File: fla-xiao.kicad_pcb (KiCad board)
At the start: 2 copper layers, 49.7 x 30.7 mm, 9 parts, among them J3 Conn_PinHeader_2x03_P2.54mm_V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, J4 Conn_PinHeader_1x08_P2.54mm_H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, J5 Conn_PinHeader_1x05_P2.54mm_H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, M1 Module_XIAO-RP2040_SocketSMD, SW1 BUTTON_B3SN

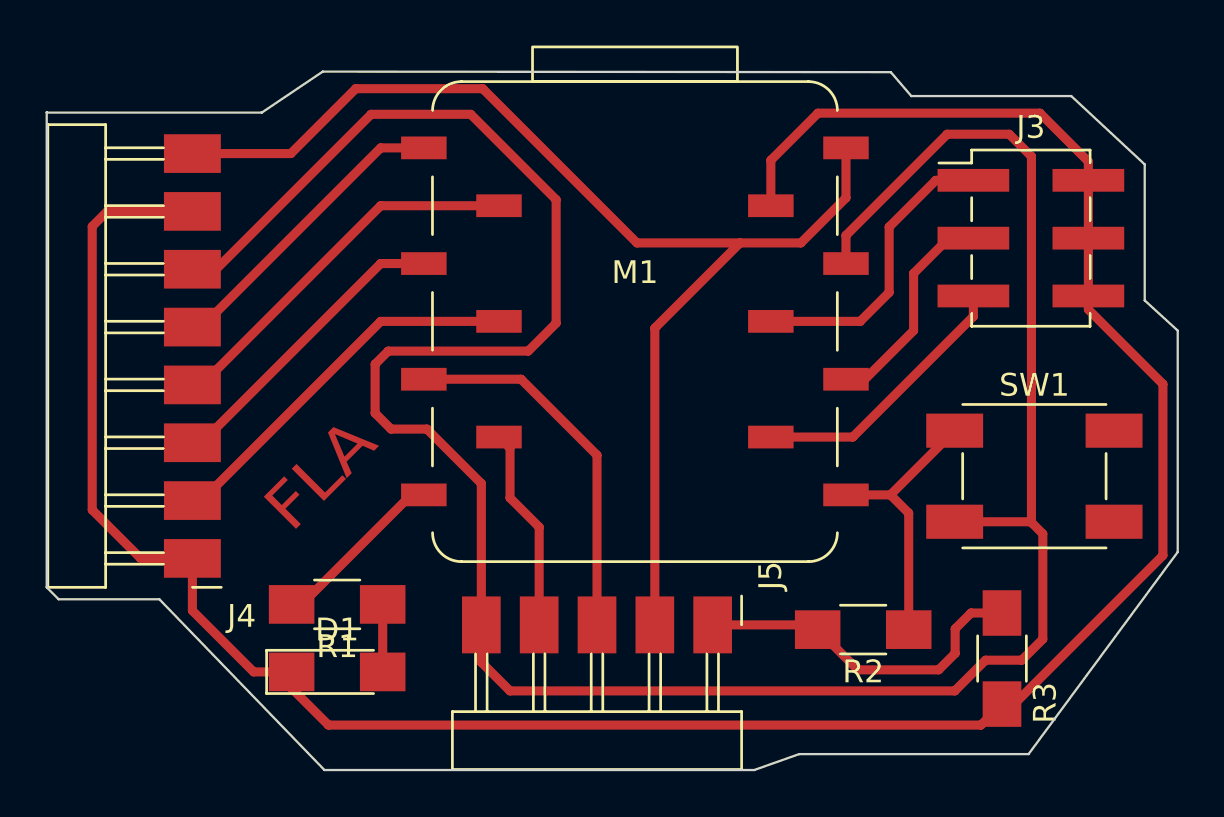
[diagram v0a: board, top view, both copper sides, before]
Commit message: Adjust trace and updated image
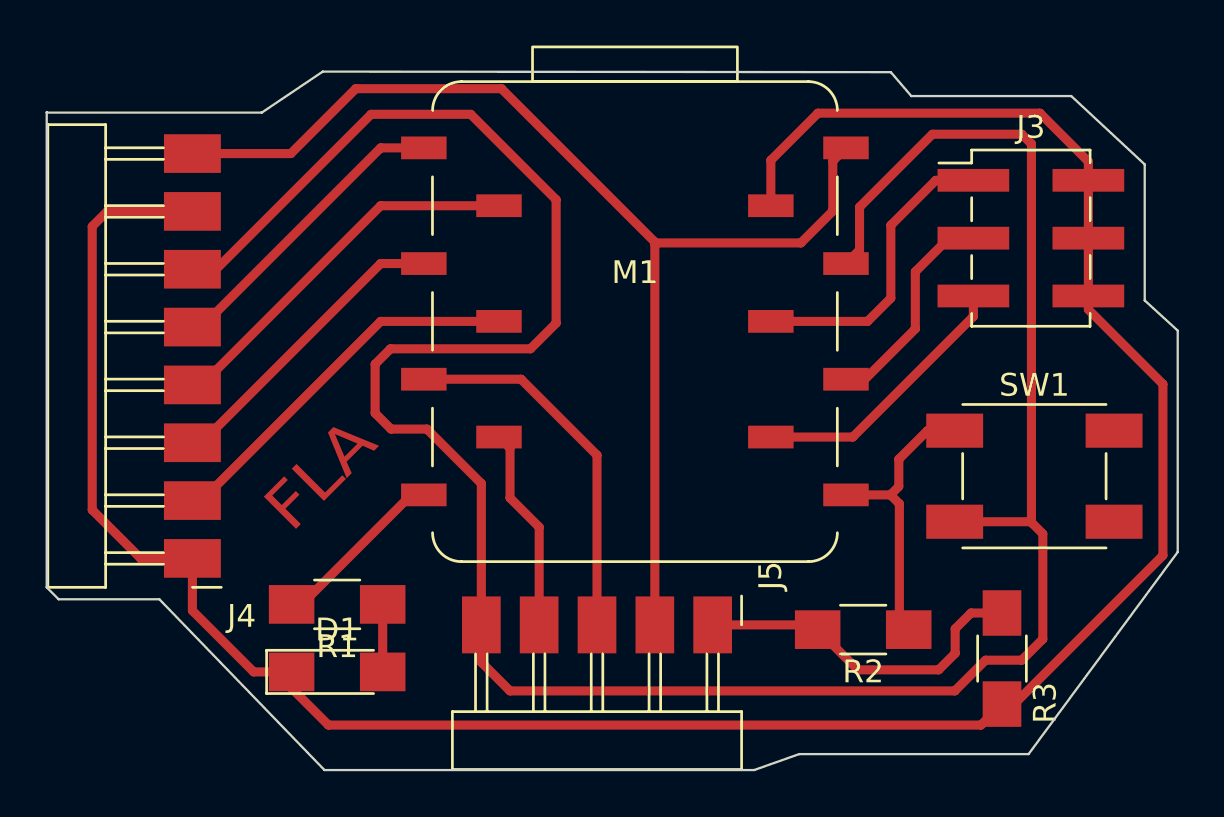
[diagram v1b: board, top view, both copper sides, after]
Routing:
- net PWR_5V: track 54.0 -> 52.5 mm
- net PWR_3V3: track 113.4 -> 114.2 mm
- net A7: track 12.2 -> 12.9 mm
